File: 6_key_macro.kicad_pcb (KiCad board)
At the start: 2 copper layers, 85 x 55 mm, 39 parts, among them J1 SWD, P1 USB_C_Plug_USB2.0, Q1 DMG1012T, SW1 CherryMX_LED, SW2 CherryMX_LED, SW3 CherryMX_LED, SW4 CherryMX_LED, SW5 CherryMX_LED, SW6 CherryMX_LED, SW7 Boot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

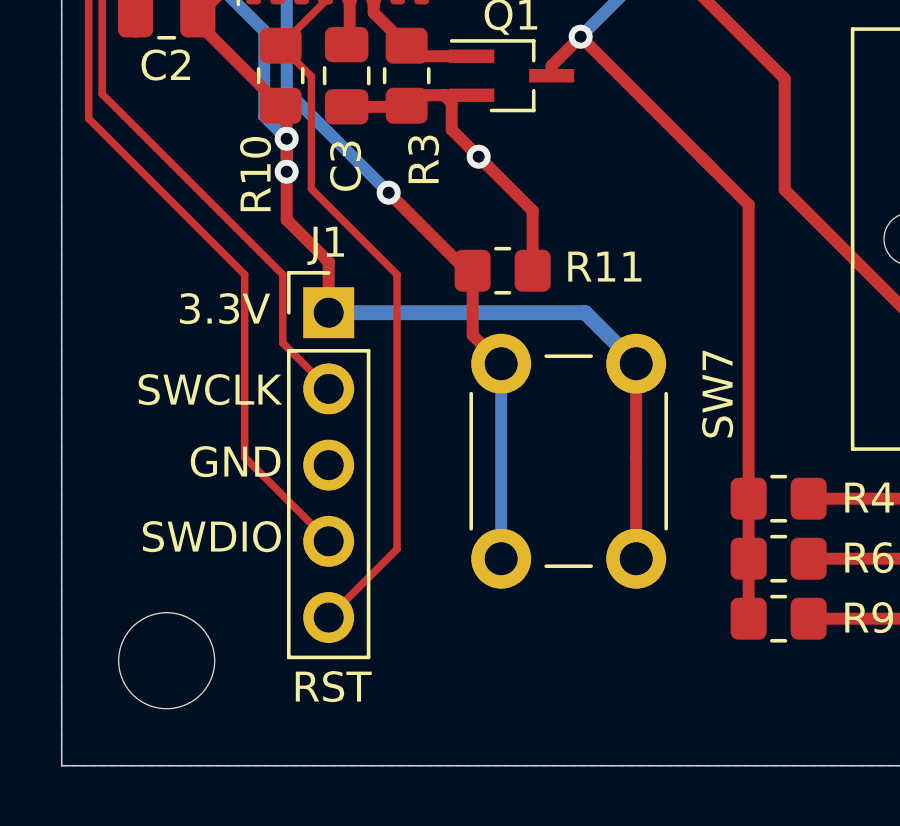
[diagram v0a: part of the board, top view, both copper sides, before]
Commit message: moved files to top level. Decided to move firmware to separate repo
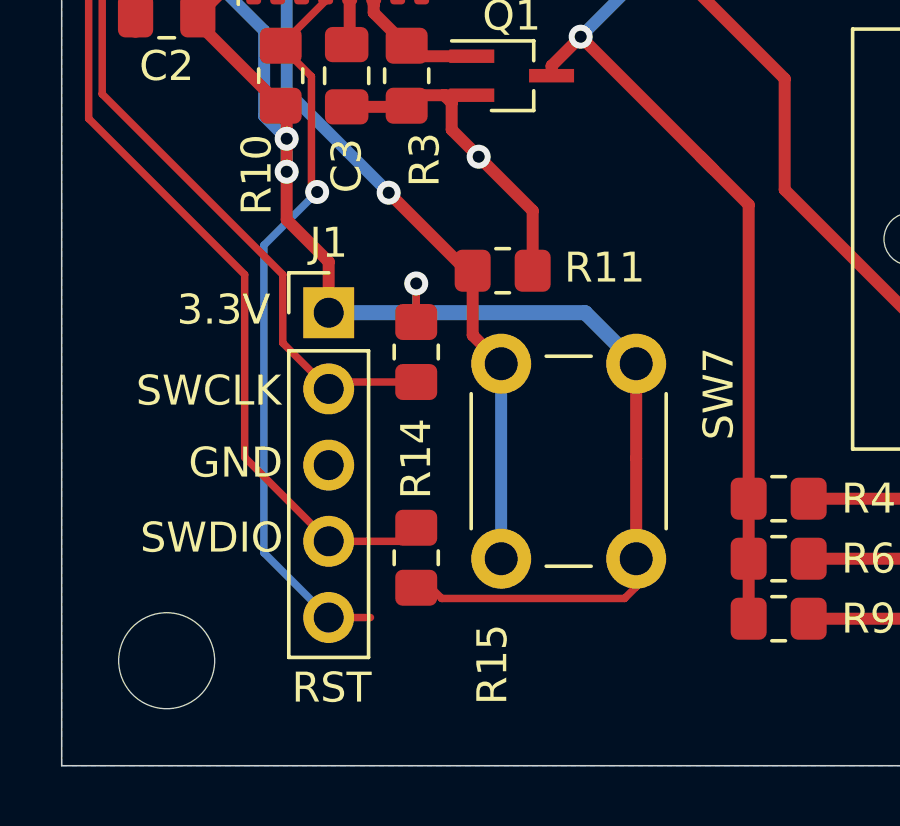
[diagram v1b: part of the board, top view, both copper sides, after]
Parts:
- added R14: 10k, Resistor_SMD:R_0805_2012Metric_Pad1.20x1.40mm_HandSolder, F.Cu at (67.8, 156.2)
- added R15: 10k, Resistor_SMD:R_0805_2012Metric_Pad1.20x1.40mm_HandSolder, F.Cu at (67.8, 163.1)
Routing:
- net +3V3: track 80.4 -> 91.3 mm, vias 4 -> 5
- net /SWDIO: track 36.7 -> 39.8 mm
- net /SWCLK: track 28.7 -> 31.7 mm
- net /Reset: track 24.4 -> 25.2 mm, vias 0 -> 1

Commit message: update files to kicad V6
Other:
- net class Default removed
